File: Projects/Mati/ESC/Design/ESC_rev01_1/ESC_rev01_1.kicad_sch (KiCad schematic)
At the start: 0 parts

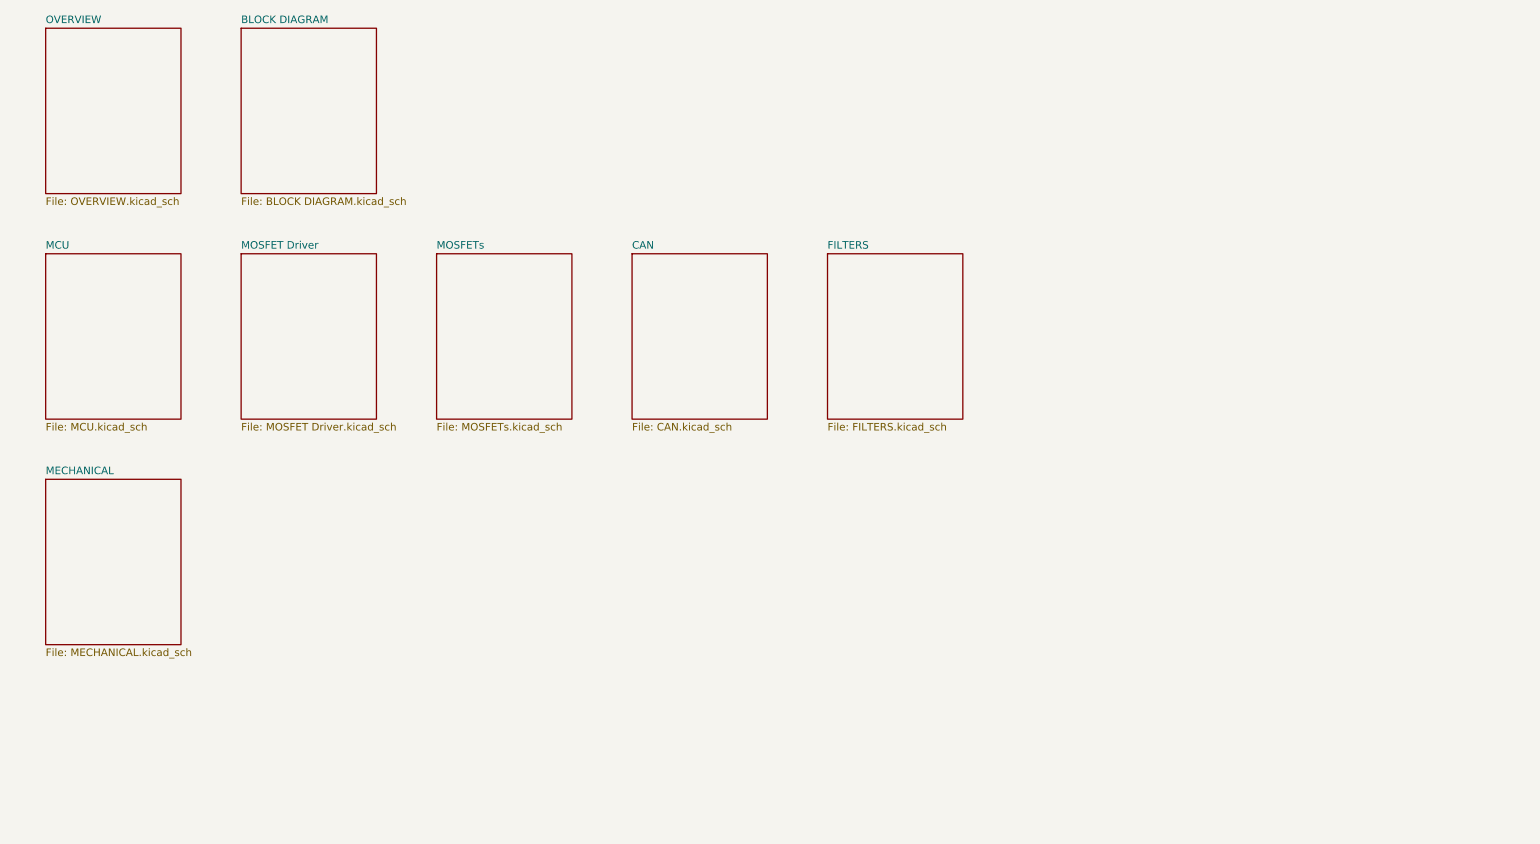
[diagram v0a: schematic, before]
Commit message: Update 03
STM32F4 MCU Schematic Design
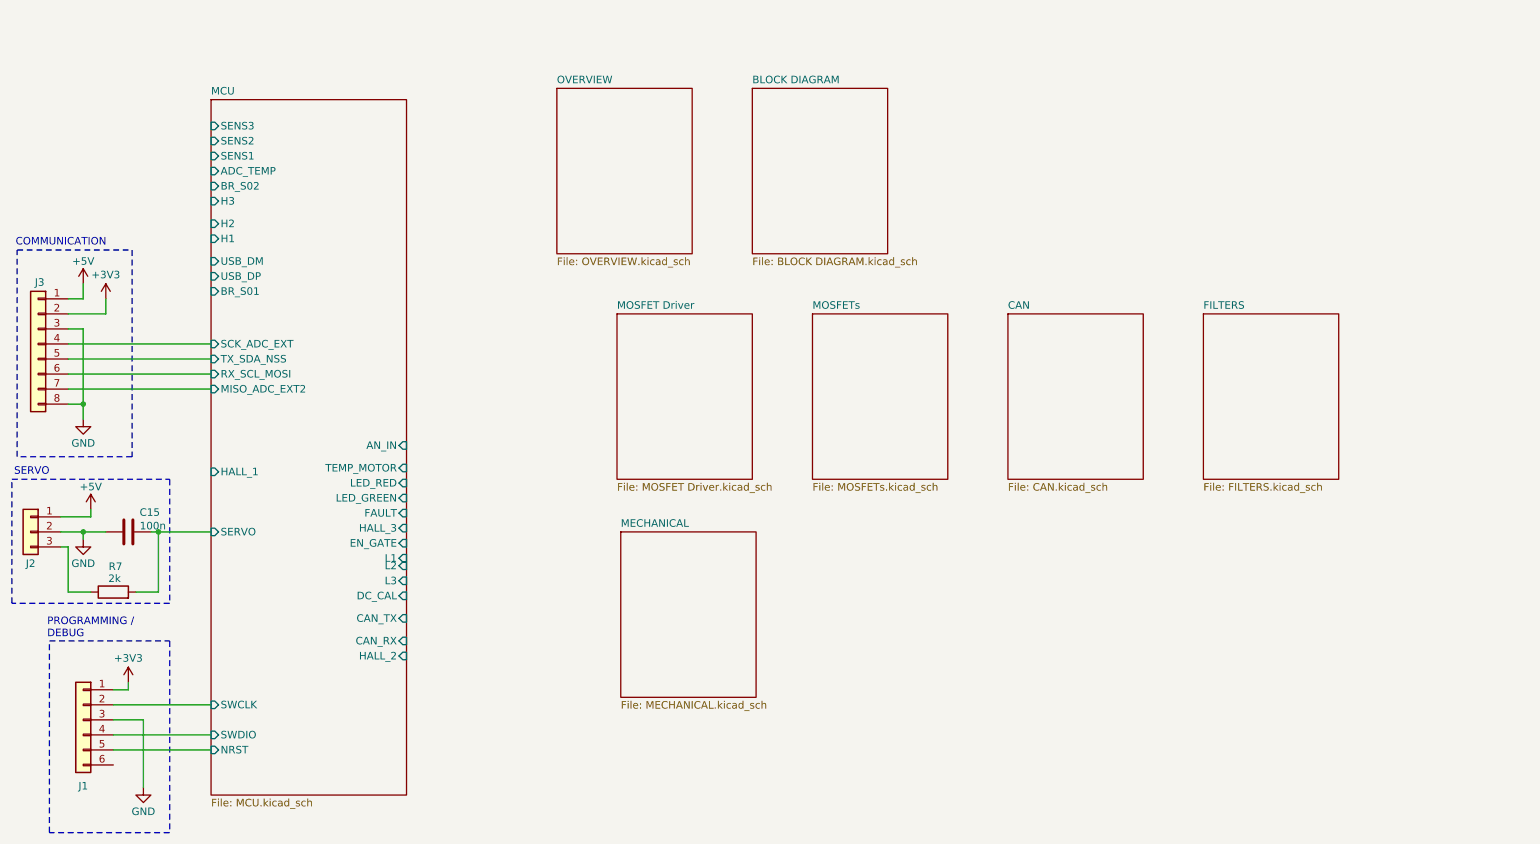
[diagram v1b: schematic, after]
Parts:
- added C15: 100n, symbol Device:C
- added J1: Conn_01x06, symbol Connector_Generic:Conn_01x06
- added J2: Conn_01x03, symbol Connector_Generic:Conn_01x03
- added J3: Conn_01x08, symbol Connector_Generic:Conn_01x08
- added R7: 2k, symbol Device:R
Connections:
- new net: J2.3 (Pin_3), R7.1
- new net +3V3: J1.1 (Pin_1), J3.2 (Pin_2)
- new net +5V: J2.1 (Pin_1), J3.1 (Pin_1)
- new net GND: C15.1, J1.3 (Pin_3), J2.2 (Pin_2), J3.3 (Pin_3), J3.8 (Pin_8)
- new net MCU/MISO_ADC_EXT2: J3.7 (Pin_7)
- new net MCU/NRST: J1.5 (Pin_5)
- new net MCU/RX_SCL_MOSI: J3.6 (Pin_6)
- new net MCU/SCK_ADC_EXT: J3.4 (Pin_4)
- new net MCU/SERVO: C15.2, R7.2
- new net MCU/SWCLK: J1.2 (Pin_2)
- new net MCU/SWDIO: J1.4 (Pin_4)
- new net MCU/TX_SDA_NSS: J3.5 (Pin_5)
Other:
- sheet MCU ports: added ADC_TEMP, AN_IN, BR_S01, BR_S02, CAN_RX, CAN_TX, DC_CAL, EN_GATE, FAULT, H1, H2, H3, HALL_1, HALL_2, HALL_3, L1, L2, L3, LED_GREEN, LED_RED, MISO_ADC_EXT2, NRST, RX_SCL_MOSI, SCK_ADC_EXT, SENS1, SENS2, SENS3, SERVO, SWCLK, SWDIO, TEMP_MOTOR, TX_SDA_NSS, USB_DM, USB_DP; removed none
- note added: "COMMUNICATION"
- note added: "PROGRAMMING / DEBUG"
- note added: "SERVO"

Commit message: Update 06
USB, CAN Bus, TVS, and Schematic Completion
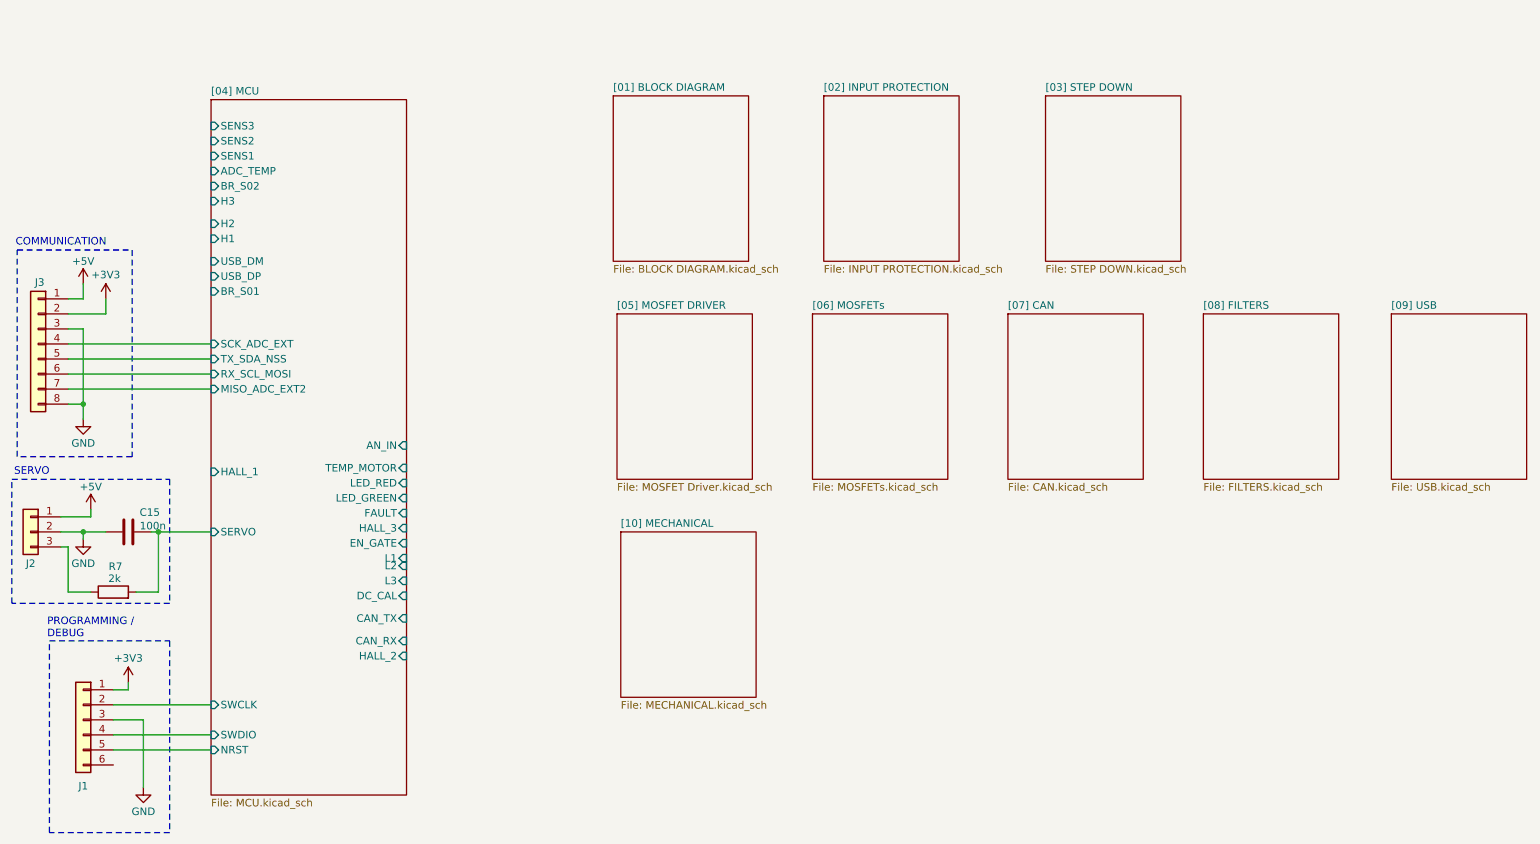
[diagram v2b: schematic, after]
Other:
- sheet BLOCK DIAGRAM renamed [01] BLOCK DIAGRAM
- sheet CAN renamed [07] CAN
- sheet FILTERS renamed [08] FILTERS
- sheet MCU renamed [04] MCU
- sheet MECHANICAL renamed [10] MECHANICAL
- sheet MOSFET Driver renamed [05] MOSFET DRIVER
- sheet MOSFETs renamed [06] MOSFETs
- sheet OVERVIEW renamed [09] USB
- added sheet [02] INPUT PROTECTION (INPUT PROTECTION.kicad_sch)
- added sheet [03] STEP DOWN (STEP DOWN.kicad_sch)
- sheet [09] USB: file OVERVIEW.kicad_sch -> USB.kicad_sch
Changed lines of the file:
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@@
 	)
 	(sheet
-		(at 116.84 31.75)
-		(size 22.86 27.94)
-		(fields_autoplaced yes)
-		(stroke
-			(width 0.1524)
-			(type solid)
-		)
-		(fill
-			(color 0 0 0 0.0000)
-		)
-		(property "Sheetname" "OVERVIEW"
-			(at 116.84 31.0384 0)
-			(effects
-				(font
-					(size 1.27 1.27)
-				)
-				(justify left bottom)
-			)
-		)
-		(property "Sheetfile" "OVERVIEW.kicad_sch"
-			(at 116.84 60.2746 0)
-			(effects
-				(font
-					(size 1.27 1.27)
-				)
-				(justify left top)
-			)
-		)
-		(instances
-			(project "ESC_rev01_1"
-				(path "/f8b31c4e-d526-42a0-803b-62608aba82c2"
-					(page "7")
+		(at 257.81 69.85)
+		(size 22.86 27.94)
+		(fields_autoplaced yes)
+		(stroke
+			(width 0.1524)
+			(type solid)
+		)
+		(fill
+			(color 0 0 0 0.0000)
+		)
+		(property "Sheetname" "[09] USB"
+			(at 257.81 69.1384 0)
+			(effects
+				(font
+					(size 1.27 1.27)
+				)
+				(justify left bottom)
+			)
+		)
+		(property "Sheetfile" "USB.kicad_sch"
+			(at 257.81 98.3746 0)
+			(effects
+				(font
+					(size 1.27 1.27)
+				)
+				(justify left top)
+			)
+		)
+		(instances
+			(project "ESC_rev01_1"
+				(path "/f8b31c4e-d526-42a0-803b-62608aba82c2"
+					(page "09")
 				)
 			)
@@
 			(color 0 0 0 0.0000)
 		)
-		(property "Sheetname" "FILTERS"
+		(property "Sheetname" "[08] FILTERS"
 			(at 226.06 69.1384 0)
 			(effects
@@
 			(project "ESC_rev01_1"
 				(path "/f8b31c4e-d526-42a0-803b-62608aba82c2"
-					(page "6")
-				)
-			)
-		)
-	)
-	(sheet
-		(at 149.86 31.75)
-		(size 22.86 27.94)
-		(fields_autoplaced yes)
-		(stroke
-			(width 0.1524)
-			(type solid)
-		)
-		(fill
-			(color 0 0 0 0.0000)
-		)
-		(property "Sheetname" "BLOCK DIAGRAM"
-			(at 149.86 31.0384 0)
+					(page "08")
+				)
+			)
+		)
+	)
+	(sheet
+		(at 126.365 33.02)
+		(size 22.86 27.94)
+		(fields_autoplaced yes)
+		(stroke
+			(width 0.1524)
+			(type solid)
+		)
+		(fill
+			(color 0 0 0 0.0000)
+		)
+		(property "Sheetname" "[01] BLOCK DIAGRAM"
+			(at 126.365 32.3084 0)
 			(effects
 				(font
@@
 		)
 		(property "Sheetfile" "BLOCK DIAGRAM.kicad_sch"
-			(at 149.86 60.2746 0)
-			(effects
-				(font
-					(size 1.27 1.27)
-				)
-				(justify left top)
-			)
-		)
-		(instances
-			(project "ESC_rev01_1"
-				(path "/f8b31c4e-d526-42a0-803b-62608aba82c2"
-					(page "8")
+			(at 126.365 61.5446 0)
+			(effects
+				(font
+					(size 1.27 1.27)
+				)
+				(justify left top)
+			)
+		)
+		(instances
+			(project "ESC_rev01_1"
+				(path "/f8b31c4e-d526-42a0-803b-62608aba82c2"
+					(page "01")
+				)
+			)
+		)
+	)
+	(sheet
+		(at 161.925 33.02)
+		(size 22.86 27.94)
+		(fields_autoplaced yes)
+		(stroke
+			(width 0.1524)
+			(type solid)
+		)
+		(fill
+			(color 0 0 0 0.0000)
+		)
+		(property "Sheetname" "[02] INPUT PROTECTION"
+			(at 161.925 32.3084 0)
+			(effects
+				(font
+					(size 1.27 1.27)
+				)
+				(justify left bottom)
+			)
+		)
+		(property "Sheetfile" "INPUT PROTECTION.kicad_sch"
+			(at 161.925 61.5446 0)
+			(effects
+				(font
+					(size 1.27 1.27)
+				)
+				(justify left top)
+			)
+		)
+		(instances
+			(project "ESC_rev01_1"
+				(path "/f8b31c4e-d526-42a0-803b-62608aba82c2"
+					(page "02")
 				)
 			)
@@
 			(color 0 0 0 0.0000)
 		)
-		(property "Sheetname" "MECHANICAL"
+		(property "Sheetname" "[10] MECHANICAL"
 			(at 127.635 105.9684 0)
 			(effects
@@
 			(project "ESC_rev01_1"
 				(path "/f8b31c4e-d526-42a0-803b-62608aba82c2"
-					(page "9")
+					(page "10")
 				)
 			)
@@
 			(color 0 0 0 0.0000)
 		)
-		(property "Sheetname" "CAN"
+		(property "Sheetname" "[07] CAN"
 			(at 193.04 69.1384 0)
 			(effects
@@
 			(project "ESC_rev01_1"
 				(path "/f8b31c4e-d526-42a0-803b-62608aba82c2"
-					(page "5")
+					(page "07")
 				)
 			)
@@
 			(color 0 0 0 0.0000)
 		)
-		(property "Sheetname" "MOSFETs"
+		(property "Sheetname" "[06] MOSFETs"
 			(at 160.02 69.1384 0)
 			(effects
@@
 			(project "ESC_rev01_1"
 				(path "/f8b31c4e-d526-42a0-803b-62608aba82c2"
-					(page "4")
+					(page "06")
 				)
 			)
@@
 			(color 0 0 0 0.0000)
 		)
-		(property "Sheetname" "MCU"
+		(property "Sheetname" "[04] MCU"
 			(at 58.42 32.9434 0)
 			(effects
@@
 			(project "ESC_rev01_1"
 				(path "/f8b31c4e-d526-42a0-803b-62608aba82c2"
-					(page "2")
+					(page "04")
 				)
 			)
@@
 			(color 0 0 0 0.0000)
 		)
-		(property "Sheetname" "MOSFET Driver"
+		(property "Sheetname" "[05] MOSFET DRIVER"
 			(at 127 69.1384 0)
 			(effects
@@
 			(project "ESC_rev01_1"
 				(path "/f8b31c4e-d526-42a0-803b-62608aba82c2"
-					(page "3")
-				)
-			)
+					(page "05")
+				)
+			)
+		)
+	)
+	(sheet
+		(at 199.39 33.02)
+		(size 22.86 27.94)
+		(fields_autoplaced yes)
+		(stroke
+			(width 0.1524)
+			(type solid)
+		)
+		(fill
+			(color 0 0 0 0.0000)
+		)
+		(property "Sheetname" "[03] STEP DOWN"
+			(at 199.39 32.3084 0)
+			(effects
+				(font
+					(size 1.27 1.27)
+				)
+				(justify left bottom)
+			)
+		)
+		(property "Sheetfile" "STEP DOWN.kicad_sch"
+			(at 199.39 61.5446 0)
+			(effects
+				(font
+					(size 1.27 1.27)
+				)
+				(justify left top)
+			)
+		)
+		(instances
+			(project "ESC_rev01_1"
+				(path "/f8b31c4e-d526-42a0-803b-62608aba82c2"
+					(page "03")
+				)
+			)
